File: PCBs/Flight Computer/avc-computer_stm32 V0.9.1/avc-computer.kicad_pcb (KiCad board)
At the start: 2 copper layers, 57.8 x 87.2 mm, 54 parts, among them IC1 MP2307, J1 Conn_ARM_JTAG_SWD_10, J2 Conn_01x02_Female, J3 ESP_01_Socket, J4 ESC Power, J5 ESC Connector, J6 OLED Display, U1 CAT24M01W, U2 CAT24M01W, U3 STM32F103C8Tx, U4 BNO085, U5 CAT24M01W, U6 CAT24M01W, U7 LD1117S33TR_SOT223, U8 BMP581

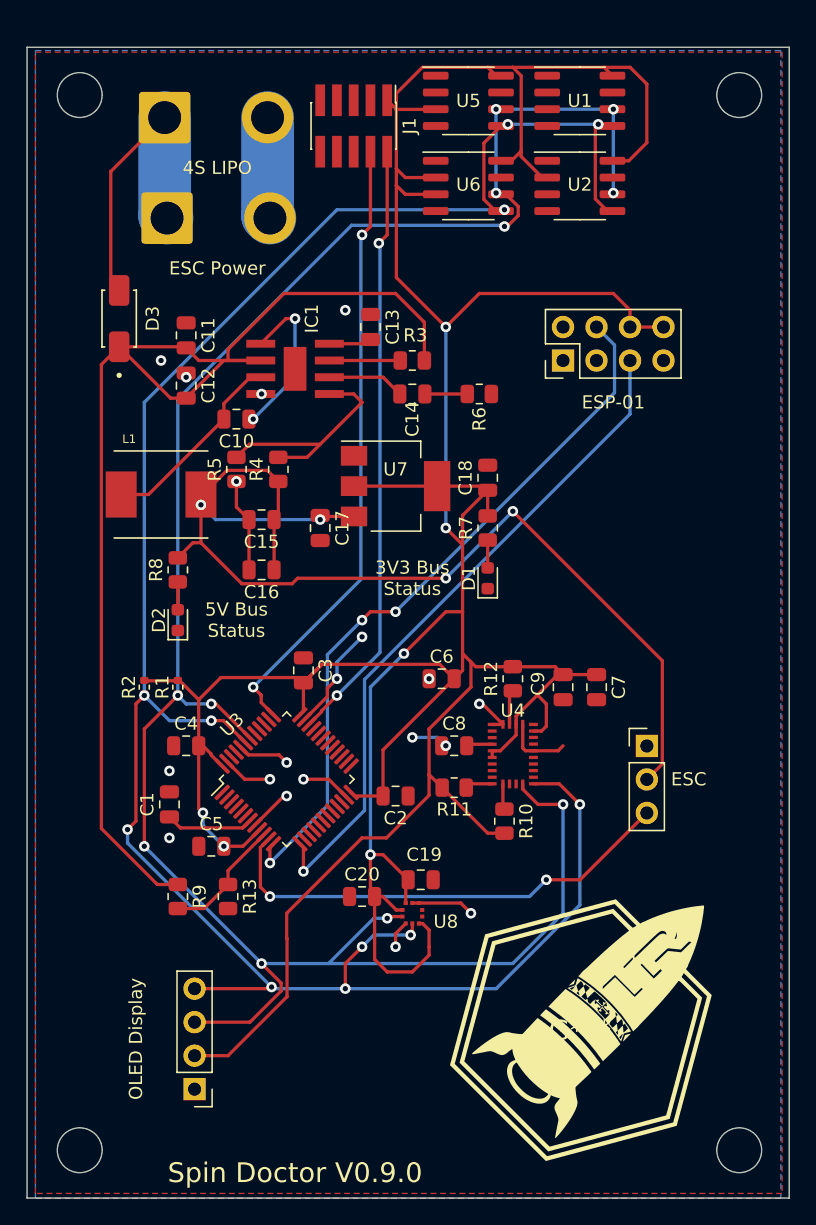
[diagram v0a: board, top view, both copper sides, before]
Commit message: Fixed all issues except for 5v buck inductor heating
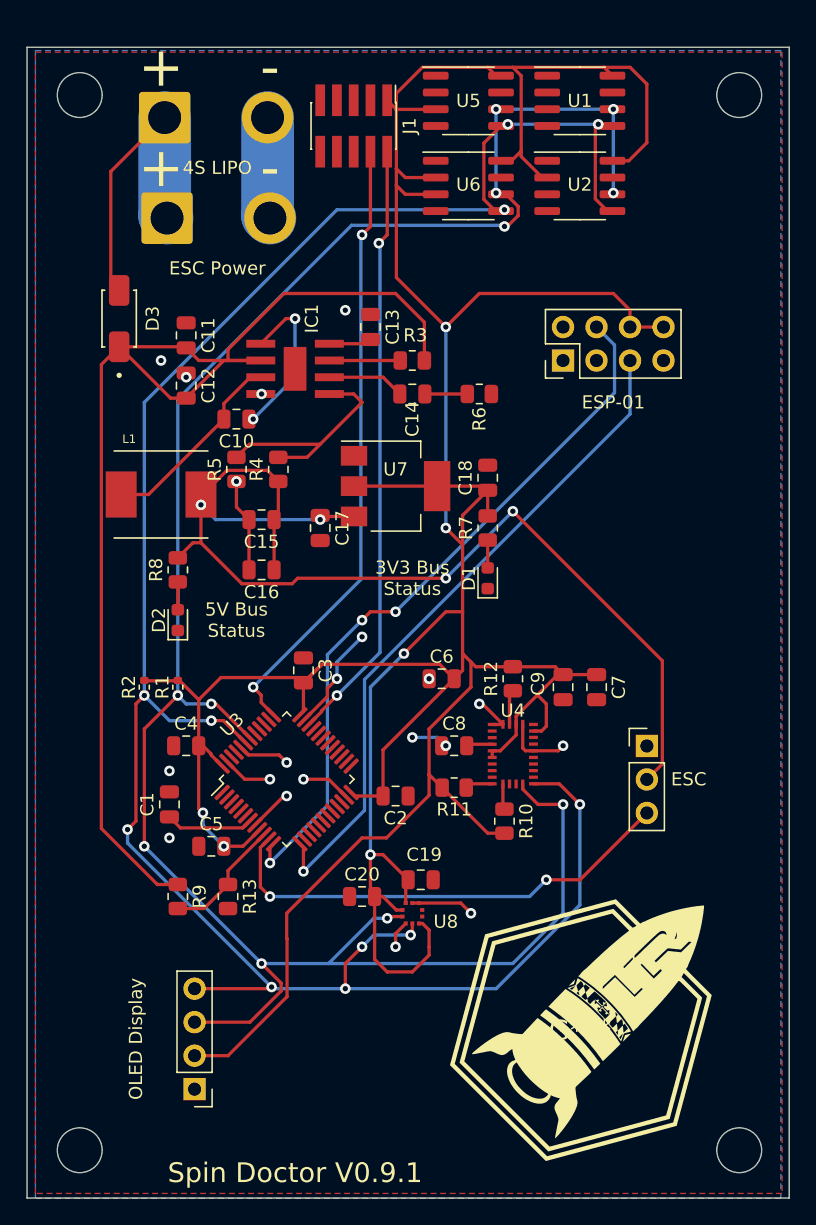
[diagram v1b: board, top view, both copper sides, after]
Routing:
- net GND: vias 19 -> 20
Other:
- board text added: "+"
- board text added: "-"
- board text added: "Spin Doctor V0.9.1"
- board text removed: "Spin Doctor V0.9.0"
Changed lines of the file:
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@@
     (effects (font (size 1 1) (thickness 0.15)))
+  )
+  (gr_text "+" (at 103.505 64.77) (layer "F.SilkS")
+    (effects (font (size 3 3) (thickness 0.15)))
+  )
+  (gr_text "-" (at 111.76 64.77) (layer "F.SilkS")
+    (effects (font (size 3 3) (thickness 0.15)))
   )
   (gr_text "5V Bus\nStatus" (at 109.22 99.06) (layer "F.SilkS")
     (effects (font (size 1 1) (thickness 0.15)))
   )
-  (gr_text "Spin Doctor V0.9.0" (at 113.665 140.97) (layer "F.SilkS")
+  (gr_text "Spin Doctor V0.9.1" (at 113.665 140.97) (layer "F.SilkS")
     (effects (font (size 1.5 1.5) (thickness 0.3)))
   )
   (gr_text "3V3 Bus\nStatus" (at 122.555 95.885) (layer "F.SilkS")
     (effects (font (size 1 1) (thickness 0.15)))
+  )
+  (gr_text "-" (at 111.76 57.15) (layer "F.SilkS")
+    (effects (font (size 3 3) (thickness 0.15)))
   )
   (gr_text "ESP-01" (at 137.795 82.55) (layer "F.SilkS")
@@
   (gr_text "OLED Display" (at 101.6 130.81 90) (layer "F.SilkS")
     (effects (font (size 1 1) (thickness 0.15)))
+  )
+  (gr_text "+" (at 103.505 57.15) (layer "F.SilkS")
+    (effects (font (size 3 3) (thickness 0.15)))
   )
   (segment (start 110.175 91.44) (end 109.22 90.485) (width 0.25) (layer "F.Cu") (net 1))
@@
   (via (at 113.03 109.855) (size 0.8) (drill 0.4) (layers "F.Cu" "B.Cu") (free) (net 1))
   (via (at 111.125 81.915) (size 0.8) (drill 0.4) (layers "F.Cu" "B.Cu") (net 1))
+  (via (at 133.985 108.585) (size 0.8) (drill 0.4) (layers "F.Cu" "B.Cu") (net 1))
   (via (at 104.14 110.49) (size 0.8) (drill 0.4) (layers "F.Cu" "B.Cu") (free) (net 1))
   (via (at 117.475 75.565) (size 0.8) (drill 0.4) (layers "F.Cu" "B.Cu") (net 1))

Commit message: Fixed all issues except for 5v buck inductor heating
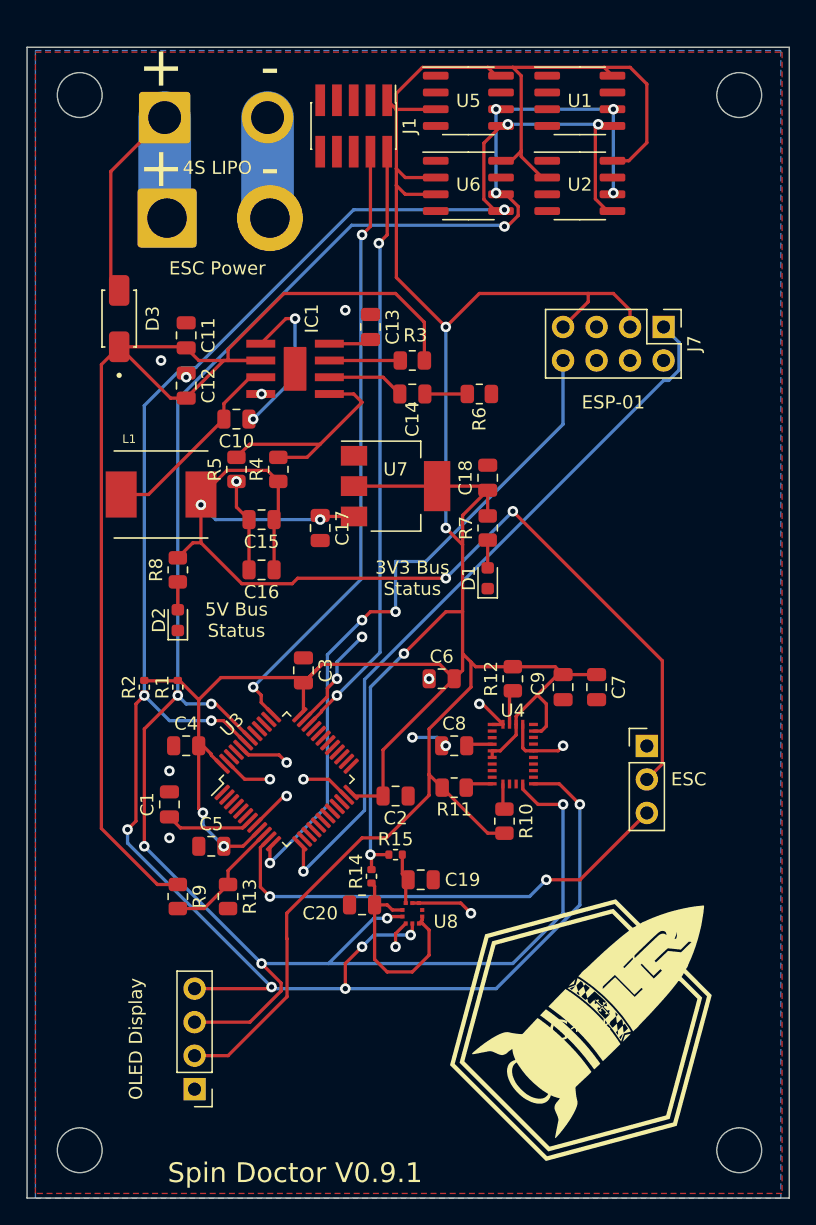
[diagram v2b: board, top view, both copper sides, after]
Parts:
- removed J3: ESP_01_Socket, Connector_PinHeader_2.54mm:PinHeader_2x04_P2.54mm_Vertical
- added J7: Conn_02x04_Odd_Even, Connector_PinHeader_2.54mm:PinHeader_2x04_P2.54mm_Vertical, F.Cu at (141.6, 76.8)
- added R14: 10, Resistor_SMD:R_0402_1005Metric, F.Cu at (119.5, 118.5)
- added R15: 10, Resistor_SMD:R_0402_1005Metric, F.Cu at (121.3, 116.8)
- R13: value 198 -> 200
- moved C20 0.64 mm to (118.7, 120.7)
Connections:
- C19 pad 2: +3V3 -> Net-(U8-VDD)
- C20 pad 2: +3V3 -> Net-(U8-CSB)
- U8 pad 1: +3V3 -> Net-(U8-CSB)
- U8 pad 10: +3V3 -> Net-(U8-VDD)
- U8 pad 5: +3V3 -> Net-(U8-CSB)
- U8 pad 6: unconnected-(U8-Pad6) -> Net-(U8-CSB)
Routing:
- net +3V3: track 315.6 -> 295.0 mm
- net Net-(U8-CSB): track 0.00 -> 16.7 mm
- net /Microcontroller/PA3: track 51.2 -> 56.0 mm
- net Net-(U8-VDD): track 0.00 -> 3.93 mm
- net /Microcontroller/PA2: track 54.7 -> 51.3 mm
